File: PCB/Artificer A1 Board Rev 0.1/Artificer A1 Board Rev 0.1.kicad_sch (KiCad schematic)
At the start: 0 parts

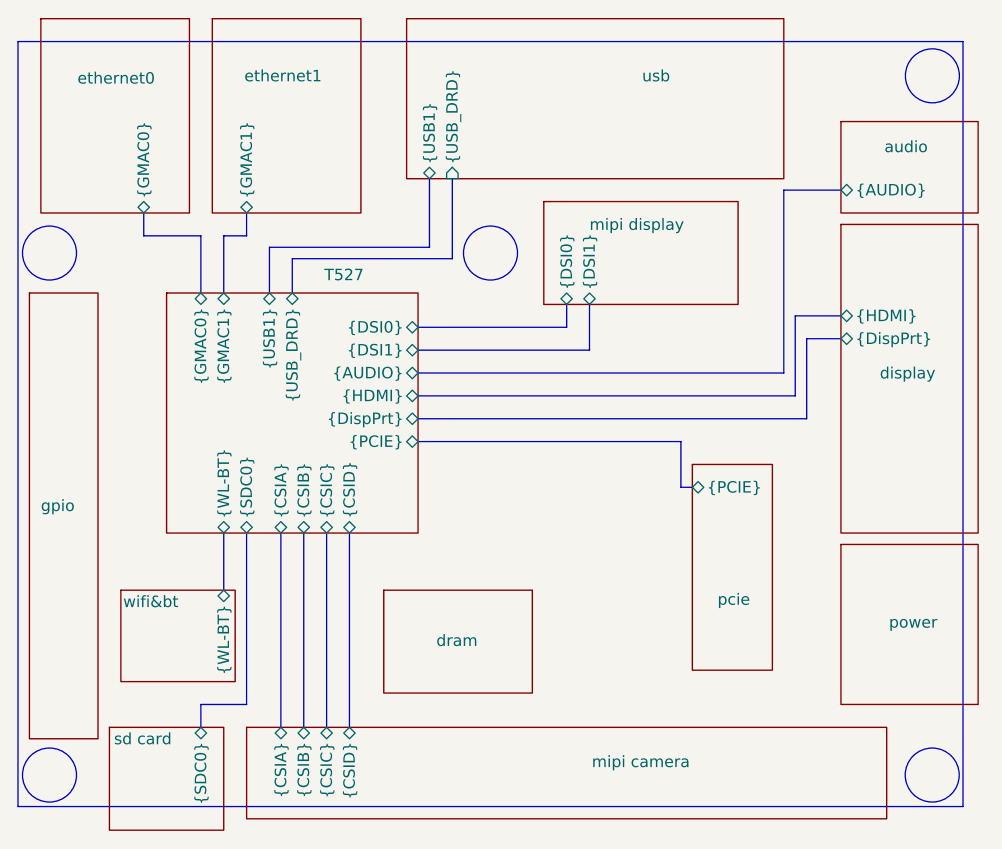
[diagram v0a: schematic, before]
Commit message: cleaned up, kicad 10 & usb c pd
migrated to Kicad 10,
added USB PD for power input
added capacitors inductors and resistor footprints
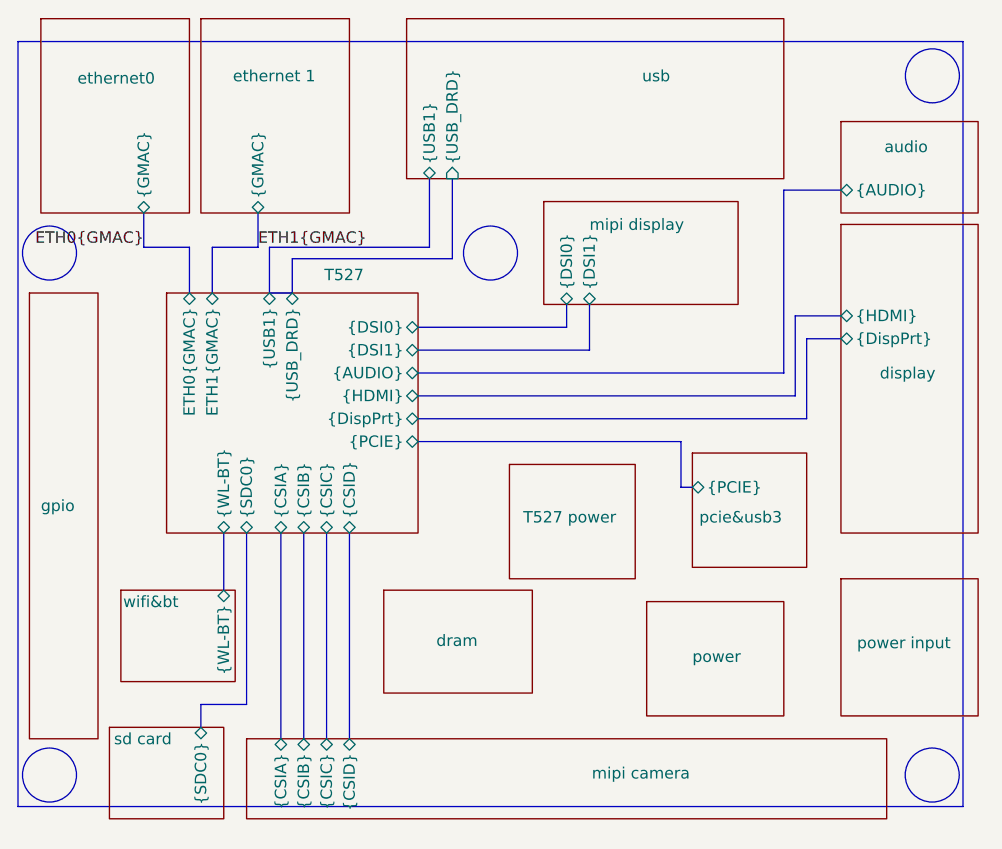
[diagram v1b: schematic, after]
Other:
- sheet pcie renamed pcie&usb3
- removed sheet ethernet1
- added sheet T527 power (T527 power.kicad_sch)
- added sheet ethernet 1 (ethernet0.kicad_sch)
- added sheet power input (power input.kicad_sch)
- sheet T527 ports: added ETH0{GMAC}, ETH1{GMAC}; removed {GMAC0}, {GMAC1}
- sheet ethernet0 ports: added {GMAC}; removed {GMAC0}
- sheet pcie&usb3: file pcie.kicad_sch -> pcie&usb3.kicad_sch
